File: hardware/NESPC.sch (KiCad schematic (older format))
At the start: 18 parts, among them J0 NESCART, J3 EXPANSION, J6 JTAG, U2 CLONE CIC, U3 ATF1508, U5 512Kx8 SRAM PRG, U6 512Kx8 FLASH PRG, U7 512Kx8 SRAM CHR, U8 512Kx8 FLASH CHR

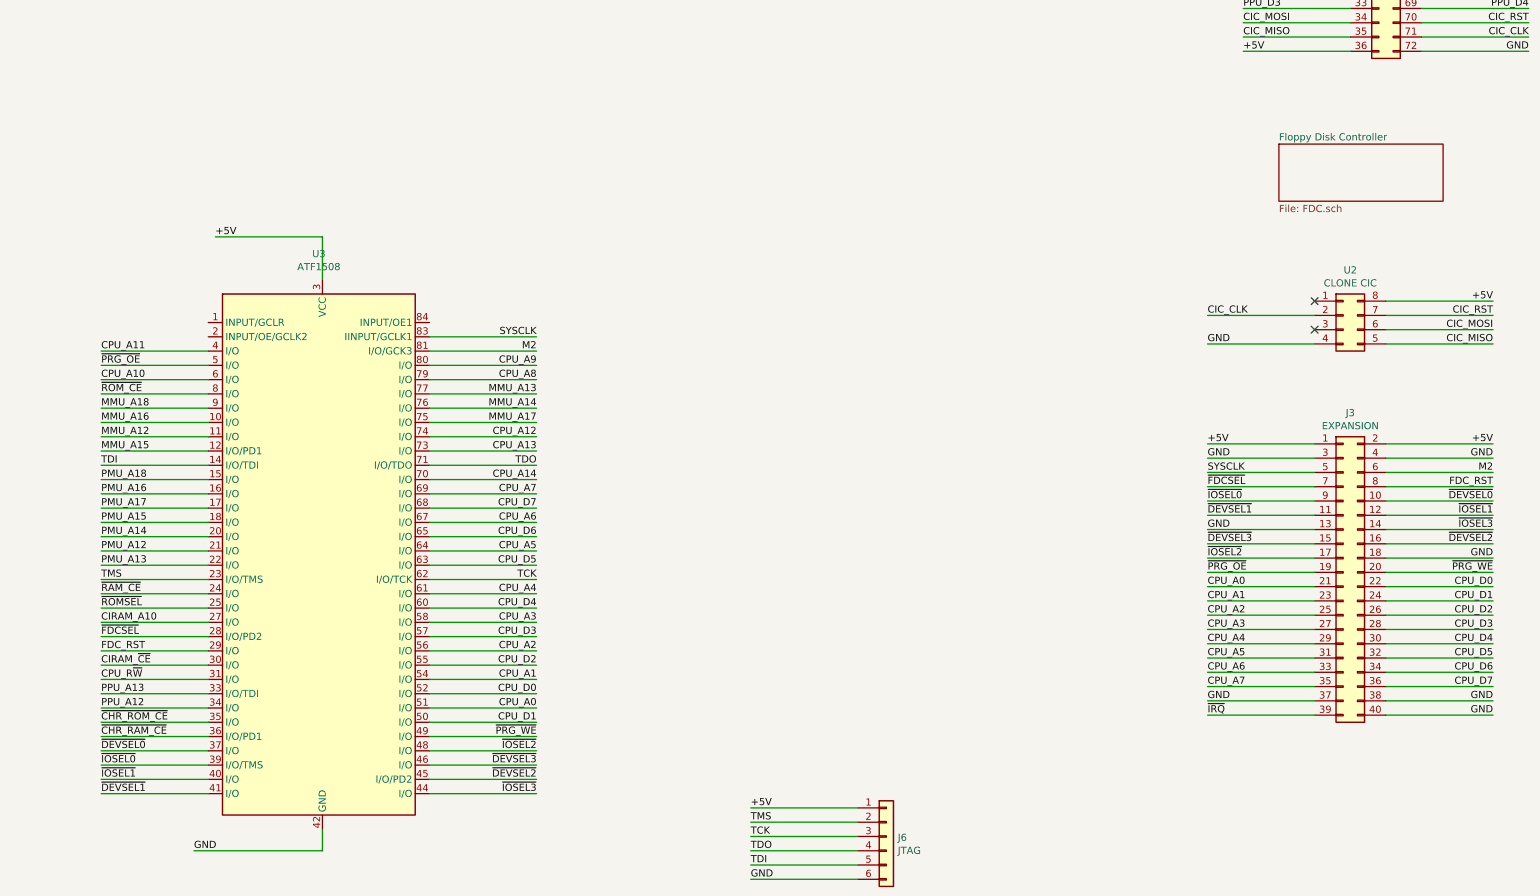
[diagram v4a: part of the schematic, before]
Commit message: Intel 82077 FDC and more rework
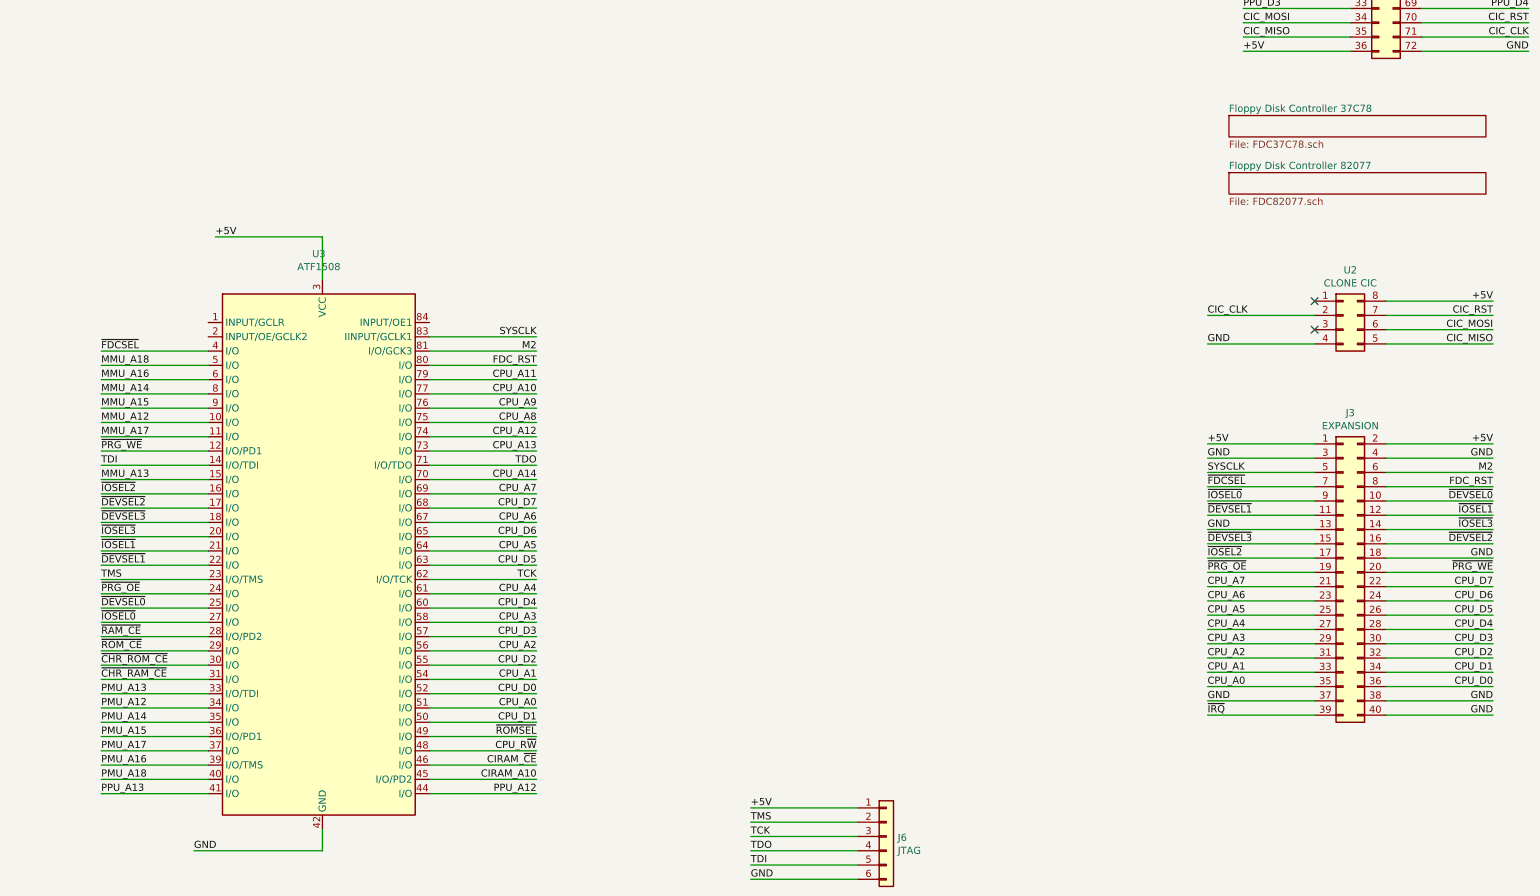
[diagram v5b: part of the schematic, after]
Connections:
- net CIRAM_A10: now also U3.45 (I/O/PD2); no longer U3.27 (I/O)
- net CIRAM_~CE: now also U3.46 (I/O); no longer U3.30 (I/O)
- net CPU_A0: now also J3.35 (Pin_35); no longer J3.21 (Pin_21)
- net CPU_A1: now also J3.33 (Pin_33); no longer J3.23 (Pin_23)
- net CPU_A10: now also U3.77 (I/O); no longer U3.6 (I/O)
- net CPU_A11: now also U3.79 (I/O); no longer U3.4 (I/O)
- net CPU_A2: now also J3.31 (Pin_31); no longer J3.25 (Pin_25)
- net CPU_A3: now also J3.29 (Pin_29); no longer J3.27 (Pin_27)
- net CPU_A4: now also J3.27 (Pin_27); no longer J3.29 (Pin_29)
- net CPU_A5: now also J3.25 (Pin_25); no longer J3.31 (Pin_31)
- net CPU_A6: now also J3.23 (Pin_23); no longer J3.33 (Pin_33)
- net CPU_A7: now also J3.21 (Pin_21); no longer J3.35 (Pin_35)
- net CPU_A8: now also U3.75 (I/O); no longer U3.79 (I/O)
- net CPU_A9: now also U3.76 (I/O); no longer U3.80 (I/O)
- net CPU_D0: now also J3.36 (Pin_36); no longer J3.22 (Pin_22)
- net CPU_D1: now also J3.34 (Pin_34); no longer J3.24 (Pin_24)
- net CPU_D2: now also J3.32 (Pin_32); no longer J3.26 (Pin_26)
- net CPU_D3: now also J3.30 (Pin_30); no longer J3.28 (Pin_28)
- net CPU_D4: now also J3.28 (Pin_28); no longer J3.30 (Pin_30)
- net CPU_D5: now also J3.26 (Pin_26); no longer J3.32 (Pin_32)
- net CPU_D6: now also J3.24 (Pin_24); no longer J3.34 (Pin_34)
- net CPU_D7: now also J3.22 (Pin_22); no longer J3.36 (Pin_36)
- net CPU_R~W: now also U3.48 (I/O); no longer U3.31 (I/O)
- net FDC_RST: now also U3.80 (I/O); no longer U3.29 (I/O)
- net MMU_A12: now also U3.10 (I/O); no longer U3.11 (I/O)
- net MMU_A13: now also U3.15 (I/O); no longer U3.77 (I/O)
- net MMU_A14: now also U3.8 (I/O); no longer U3.76 (I/O)
- net MMU_A15: now also U3.9 (I/O); no longer U3.12 (I/O/PD1)
- net MMU_A16: now also U3.6 (I/O); no longer U3.10 (I/O)
- net MMU_A17: now also U3.11 (I/O); no longer U3.75 (I/O)
- net MMU_A18: now also U3.5 (I/O); no longer U3.9 (I/O)
- net PMU_A12: now also U3.34 (I/O); no longer U3.21 (I/O)
- net PMU_A13: now also U3.33 (I/O/TDI); no longer U3.22 (I/O)
- net PMU_A14: now also U3.35 (I/O); no longer U3.20 (I/O)
- net PMU_A15: now also U3.36 (I/O/PD1); no longer U3.18 (I/O)
- net PMU_A16: now also U3.39 (I/O/TMS); no longer U3.16 (I/O)
- net PMU_A17: now also U3.37 (I/O); no longer U3.17 (I/O)
- net PMU_A18: now also U3.40 (I/O); no longer U3.15 (I/O)
- net PPU_A12: now also U3.44 (I/O); no longer U3.34 (I/O)
- net PPU_A13: now also U3.41 (I/O); no longer U3.33 (I/O/TDI)
- net ~CHR_RAM_CE: now also U3.31 (I/O); no longer U3.36 (I/O/PD1)
- net ~CHR_ROM_CE: now also U3.30 (I/O); no longer U3.35 (I/O)
- net ~DEVSEL0: now also U3.25 (I/O); no longer U3.37 (I/O)
- net ~DEVSEL1: now also U3.22 (I/O); no longer U3.41 (I/O)
- net ~DEVSEL2: now also U3.17 (I/O); no longer U3.45 (I/O/PD2)
- net ~DEVSEL3: now also U3.18 (I/O); no longer U3.46 (I/O)
- net ~FDCSEL: now also U3.4 (I/O); no longer U3.28 (I/O/PD2)
- net ~IOSEL0: now also U3.27 (I/O); no longer U3.39 (I/O/TMS)
- net ~IOSEL1: now also U3.21 (I/O); no longer U3.40 (I/O)
- net ~IOSEL2: now also U3.16 (I/O); no longer U3.48 (I/O)
- net ~IOSEL3: now also U3.20 (I/O); no longer U3.44 (I/O)
- net ~PRG_OE: now also U3.24 (I/O); no longer U3.5 (I/O)
- net ~PRG_WE: now also U3.12 (I/O/PD1); no longer U3.49 (I/O)
- net ~RAM_CE: now also U3.28 (I/O/PD2); no longer U3.24 (I/O)
- net ~ROMSEL: now also U3.49 (I/O); no longer U3.25 (I/O)
- net ~ROM_CE: now also U3.29 (I/O); no longer U3.8 (I/O)
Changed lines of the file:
@@
 $Descr USLedger 17000 11000
 encoding utf-8
-Sheet 1 2
+Sheet 1 3
 Title "NES PC"
 Date "2022-10-14"
@@
 $EndComp
 Wire Wire Line
-	14750 8300 14000 8300
-Wire Wire Line
-	14750 8400 14000 8400
-Text Label 14000 8300 0    50   ~ 0
+	14750 8600 14000 8600
+Wire Wire Line
+	14750 8500 14000 8500
+Text Label 14000 8600 0    50   ~ 0
 CPU_A2
-Text Label 14000 8400 0    50   ~ 0
+Text Label 14000 8500 0    50   ~ 0
 CPU_A3
 Wire Wire Line
+	16000 8800 15250 8800
+Wire Wire Line
+	16000 8700 15250 8700
+Wire Wire Line
+	16000 8600 15250 8600
+Wire Wire Line
+	16000 8500 15250 8500
+Wire Wire Line
+	16000 8400 15250 8400
+Wire Wire Line
+	16000 8300 15250 8300
+Wire Wire Line
+	16000 8200 15250 8200
+Wire Wire Line
 	16000 8100 15250 8100
-Wire Wire Line
-	16000 8200 15250 8200
-Wire Wire Line
-	16000 8300 15250 8300
-Wire Wire Line
-	16000 8400 15250 8400
-Wire Wire Line
-	16000 8500 15250 8500
-Wire Wire Line
-	16000 8600 15250 8600
-Wire Wire Line
-	16000 8700 15250 8700
-Wire Wire Line
-	16000 8800 15250 8800
+Text Label 16000 8100 2    50   ~ 0
+CPU_D7
+Text Label 16000 8200 2    50   ~ 0
+CPU_D6
+Text Label 16000 8300 2    50   ~ 0
+CPU_D5
+Text Label 16000 8400 2    50   ~ 0
+CPU_D4
+Text Label 16000 8500 2    50   ~ 0
+CPU_D3
+Text Label 16000 8600 2    50   ~ 0
+CPU_D2
+Text Label 16000 8700 2    50   ~ 0
+CPU_D1
 Text Label 16000 8800 2    50   ~ 0
-CPU_D7
-Text Label 16000 8700 2    50   ~ 0
-CPU_D6
-Text Label 16000 8600 2    50   ~ 0
-CPU_D5
-Text Label 16000 8500 2    50   ~ 0
-CPU_D4
-Text Label 16000 8400 2    50   ~ 0
-CPU_D3
-Text Label 16000 8300 2    50   ~ 0
-CPU_D2
-Text Label 16000 8200 2    50   ~ 0
-CPU_D1
-Text Label 16000 8100 2    50   ~ 0
 CPU_D0
 Wire Wire Line
@@
 Text Label 16000 7200 2    50   ~ 0
 GND
-Text Label 14000 8600 0    50   ~ 0
+Text Label 14000 8300 0    50   ~ 0
 CPU_A5
-Text Label 14000 8500 0    50   ~ 0
+Text Label 14000 8400 0    50   ~ 0
 CPU_A4
 Wire Wire Line
-	14750 8500 14000 8500
-Wire Wire Line
-	14750 8700 14000 8700
-Wire Wire Line
-	14750 8600 14000 8600
-Wire Wire Line
-	14750 8800 14000 8800
-Text Label 14000 8700 0    50   ~ 0
+	14750 8400 14000 8400
+Wire Wire Line
+	14750 8200 14000 8200
+Wire Wire Line
+	14750 8300 14000 8300
+Wire Wire Line
+	14750 8100 14000 8100
+Text Label 14000 8200 0    50   ~ 0
 CPU_A6
-Text Label 14000 8800 0    50   ~ 0
+Text Label 14000 8100 0    50   ~ 0
 CPU_A7
 Wire Wire Line
@@
 PPU_D4
 Wire Wire Line
-	7000 8350 6250 8350
-Text Label 6250 8350 0    50   ~ 0
+	8550 9450 9300 9450
+Text Label 9300 9450 2    50   ~ 0
 CIRAM_A10
 Wire Wire Line
@@
 PMU_A17
 Wire Wire Line
-	14750 8100 14000 8100
-Wire Wire Line
-	14750 8200 14000 8200
-Text Label 14000 8100 0    50   ~ 0
+	14750 8800 14000 8800
+Wire Wire Line
+	14750 8700 14000 8700
+Text Label 14000 8800 0    50   ~ 0
 CPU_A0
-Text Label 14000 8200 0    50   ~ 0
+Text Label 14000 8700 0    50   ~ 0
 CPU_A1
 Wire Wire Line
@@
 M2
 Wire Wire Line
-	6250 9350 7000 9350
+	6250 8350 7000 8350
+Text Label 6250 8350 0    50   ~ 0
+~IOSEL0
+Wire Wire Line
+	6250 7850 7000 7850
+Text Label 6250 7850 0    50   ~ 0
+~IOSEL1
+Wire Wire Line
+	6250 7450 7000 7450
+Text Label 6250 7450 0    50   ~ 0
+~IOSEL2
+Wire Wire Line
+	6250 8250 7000 8250
+Text Label 6250 8250 0    50   ~ 0
+~DEVSEL0
+Wire Wire Line
+	6250 7950 7000 7950
+Text Label 6250 7950 0    50   ~ 0
+~DEVSEL1
+Wire Wire Line
+	6250 7550 7000 7550
+Text Label 6250 7550 0    50   ~ 0
+~DEVSEL2
+Wire Wire Line
+	6250 6450 7000 6450
+Text Label 6250 6450 0    50   ~ 0
+~FDCSEL
+Wire Wire Line
+	7000 9250 6250 9250
+Text Label 6250 9250 0    50   ~ 0
+PMU_A17
+Wire Wire Line
+	7000 9350 6250 9350
 Text Label 6250 9350 0    50   ~ 0
-~IOSEL0
-Wire Wire Line
-	6250 9450 7000 9450
-Text Label 6250 9450 0    50   ~ 0
-~IOSEL1
-Wire Wire Line
-	9300 9250 8550 9250
-Text Label 9300 9250 2    50   ~ 0
-~IOSEL2
-Wire Wire Line
-	6250 9250 7000 9250
-Text Label 6250 9250 0    50   ~ 0
-~DEVSEL0
-Wire Wire Line
-	6250 9550 7000 9550
-Text Label 6250 9550 0    50   ~ 0
-~DEVSEL1
-Wire Wire Line
-	9300 9450 8550 9450
-Text Label 9300 9450 2    50   ~ 0
-~DEVSEL2
+PMU_A16
+Wire Wire Line
+	7000 9150 6250 9150
+Text Label 6250 9150 0    50   ~ 0
+PMU_A15
+Wire Wire Line
+	7000 8850 6250 8850
+Text Label 6250 8850 0    50   ~ 0
+PMU_A13
+Wire Wire Line
+	7000 8950 6250 8950
+Text Label 6250 8950 0    50   ~ 0
+PMU_A12
+Text Label 6250 9050 0    50   ~ 0
+PMU_A14
+Wire Wire Line
+	7000 9050 6250 9050
+Wire Wire Line
+	9300 9550 8550 9550
+Text Label 9300 9550 2    50   ~ 0
+PPU_A12
 Wire Wire Line
 	6250 8450 7000 8450
 Text Label 6250 8450 0    50   ~ 0
-~FDCSEL
-Wire Wire Line
-	7000 7550 6250 7550
-Text Label 6250 7550 0    50   ~ 0
-PMU_A17
-Wire Wire Line
-	7000 7450 6250 7450
-Text Label 6250 7450 0    50   ~ 0
-PMU_A16
-Wire Wire Line
-	7000 7650 6250 7650
-Text Label 6250 7650 0    50   ~ 0
-PMU_A15
-Wire Wire Line
-	7000 7950 6250 7950
-Text Label 6250 7950 0    50   ~ 0
-PMU_A13
-Wire Wire Line
-	7000 7850 6250 7850
-Text Label 6250 7850 0    50   ~ 0
-PMU_A12
-Text Label 6250 7750 0    50   ~ 0
-PMU_A14
-Wire Wire Line
-	7000 7750 6250 7750
-Wire Wire Line
-	6250 8950 7000 8950
-Text Label 6250 8950 0    50   ~ 0
-PPU_A12
-Wire Wire Line
-	6250 8150 7000 8150
+~RAM_CE
+Wire Wire Line
+	6250 8550 7000 8550
+Text Label 6250 8550 0    50   ~ 0
+~ROM_CE
+Wire Wire Line
+	7000 8750 6250 8750
+Text Label 6250 8750 0    50   ~ 0
+~CHR_RAM_CE
+Text Label 6250 8650 0    50   ~ 0
+~CHR_ROM_CE
+Wire Wire Line
+	6250 8650 7000 8650
+Wire Wire Line
+	7000 8150 6250 8150
 Text Label 6250 8150 0    50   ~ 0
-~RAM_CE
-Wire Wire Line
-	6250 6750 7000 6750
-Text Label 6250 6750 0    50   ~ 0
-~ROM_CE
-Wire Wire Line
-	7000 9150 6250 9150
-Text Label 6250 9150 0    50   ~ 0
-~CHR_RAM_CE
-Text Label 6250 9050 0    50   ~ 0
-~CHR_ROM_CE
-Wire Wire Line
-	6250 9050 7000 9050
-Wire Wire Line
-	7000 6550 6250 6550
-Text Label 6250 6550 0    50   ~ 0
 ~PRG_OE
 Wire Wire Line
-	8550 9150 9300 9150
-Text Label 9300 9150 2    50   ~ 0
+	7000 7150 6250 7150
+Text Label 6250 7150 0    50   ~ 0
 ~PRG_WE
 Wire Wire Line
-	6250 8650 7000 8650
-Text Label 6250 8650 0    50   ~ 0
+	9300 9350 8550 9350
+Text Label 9300 9350 2    50   ~ 0
 CIRAM_~CE
 Wire Wire Line
-	7000 8550 6250 8550
-Text Label 6250 8550 0    50   ~ 0
+	8550 6550 9300 6550
+Text Label 9300 6550 2    50   ~ 0
 FDC_RST
 Wire Wire Line
@@
 CPU_D3
 Wire Wire Line
-	8550 6550 9300 6550
-Wire Wire Line
-	7000 6650 6250 6650
-Wire Wire Line
-	7000 6450 6250 6450
-Text Label 9300 6550 2    50   ~ 0
+	8550 6850 9300 6850
+Wire Wire Line
+	8550 6750 9300 6750
+Wire Wire Line
+	8550 6650 9300 6650
+Text Label 9300 6850 2    50   ~ 0
 CPU_A9
-Text Label 6250 6650 0    50   ~ 0
+Text Label 9300 6750 2    50   ~ 0
 CPU_A10
-Text Label 6250 6450 0    50   ~ 0
+Text Label 9300 6650 2    50   ~ 0
 CPU_A11
 Wire Wire Line
-	8550 6650 9300 6650
-Text Label 9300 6650 2    50   ~ 0
+	8550 6950 9300 6950
+Text Label 9300 6950 2    50   ~ 0
 CPU_A8
 Wire Wire Line
-	6250 8250 7000 8250
-Text Label 6250 8250 0    50   ~ 0
+	9300 9150 8550 9150
+Text Label 9300 9150 2    50   ~ 0
 ~ROMSEL
+Text Label 6250 6950 0    50   ~ 0
+MMU_A12
+Wire Wire Line
+	7000 6950 6250 6950
+Text Label 6250 7350 0    50   ~ 0
+MMU_A13
+Wire Wire Line
+	7000 7350 6250 7350
+Text Label 6250 6750 0    50   ~ 0
+MMU_A14
+Wire Wire Line
+	7000 6750 6250 6750
+Text Label 6250 6850 0    50   ~ 0
+MMU_A15
+Wire Wire Line
+	7000 6850 6250 6850
 Text Label 6250 7050 0    50   ~ 0
-MMU_A12
+MMU_A17
 Wire Wire Line
 	7000 7050 6250 7050
-Text Label 9300 6750 2    50   ~ 0
-MMU_A13
-Wire Wire Line
-	8550 6750 9300 6750
-Text Label 9300 6850 2    50   ~ 0
-MMU_A14
-Wire Wire Line
-	8550 6850 9300 6850
-Text Label 6250 7150 0    50   ~ 0
-MMU_A15
-Wire Wire Line
-	7000 7150 6250 7150
-Text Label 6250 6950 0    50   ~ 0
-MMU_A16
-Wire Wire Line
-	7000 6950 6250 6950
-Text Label 9300 6950 2    50   ~ 0
-MMU_A17
-Wire Wire Line
-	8550 6950 9300 6950
-Text Label 6250 6850 0    50   ~ 0
-MMU_A18
-Wire Wire Line
-	7000 6850 6250 6850
-Wire Wire Line
-	7000 7350 6250 7350
-Text Label 6250 7350 0    50   ~ 0
+Wire Wire Line
+	7000 9450 6250 9450
+Text Label 6250 9450 0    50   ~ 0
 PMU_A18
 Wire Wire Line
-	6250 8850 7000 8850
-Text Label 6250 8850 0    50   ~ 0
+	6250 9550 7000 9550
+Text Label 6250 9550 0    50   ~ 0
 PPU_A13
 Wire Wire Line
@@
 SYSCLK
 Wire Wire Line
-	7000 8750 6250 8750
-Text Label 6250 8750 0    50   ~ 0
+	8550 9250 9300 9250
+Text Label 9300 9250 2    50   ~ 0
 CPU_R~W
 Wire Wire Line
@@
 Connection ~ 2200 8300
 Connection ~ 2200 7400
-Text Label 9300 9350 2    50   ~ 0
+Text Label 6250 7650 0    50   ~ 0
 ~DEVSEL3
 Wire Wire Line
-	9300 9350 8550 9350
-Text Label 9300 9550 2    50   ~ 0
+	6250 7650 7000 7650
+Text Label 6250 7750 0    50   ~ 0
 ~IOSEL3
 Wire Wire Line
-	9300 9550 8550 9550
+	6250 7750 7000 7750
 Wire Wire Line
 	8550 8950 9300 8950
@@
 Text Label 9300 7450 2    50   ~ 0
 CPU_A7
-$Sheet
-S 14500 5000 1150 400
-U 75E32237
-F0 "Floppy Disk Controller" 50
-F1 "FDC.sch" 50
-$EndSheet
 Wire Wire Line
 	14000 7400 14750 7400
@@
 Wire Wire Line
 	1450 6950 2650 6950
+Wire Wire Line
+	7000 6650 6250 6650
+Text Label 6250 6650 0    50   ~ 0
+MMU_A16
+Wire Wire Line
+	7000 6550 6250 6550
+Text Label 6250 6550 0    50   ~ 0
+MMU_A18
+$Sheet
+S 14150 4800 1800 150
+U 75E32237
+F0 "Floppy Disk Controller 37C78" 50
+F1 "FDC37C78.sch" 50
+$EndSheet
+$Sheet
+S 14150 5200 1800 150
+U 649831AA
+F0 "Floppy Disk Controller 82077" 50
+F1 "FDC82077.sch" 50
+$EndSheet
 $EndSCHEMATC

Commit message: Pin remapping final final final really this time
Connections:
- net TCK: now also J6.5 (Pin_5); no longer J6.3 (Pin_3)
- net TDI: now also J6.2 (Pin_2); no longer J6.5 (Pin_5)
- net TMS: now also J6.3 (Pin_3); no longer J6.2 (Pin_2)
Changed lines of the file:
@@
 	10800 9950 11550 9950
+Wire Wire Line
+	10800 10050 11550 10050
 Wire Wire Line
 	10800 9850 11550 9850
@@
 	10800 9750 11550 9750
 Wire Wire Line
-	10800 10050 11550 10050
-Wire Wire Line
 	10800 9650 11550 9650
 Text Label 10800 9650 0    50   ~ 0
 +5V
+Text Label 10800 9750 0    50   ~ 0
+TDI
+Text Label 10800 9850 0    50   ~ 0
+TMS
 Text Label 10800 10050 0    50   ~ 0
-TDI
-Text Label 10800 9750 0    50   ~ 0
-TMS
-Text Label 10800 9850 0    50   ~ 0
 TCK
 Text Label 10800 9950 0    50   ~ 0
